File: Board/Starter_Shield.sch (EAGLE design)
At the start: 12 parts

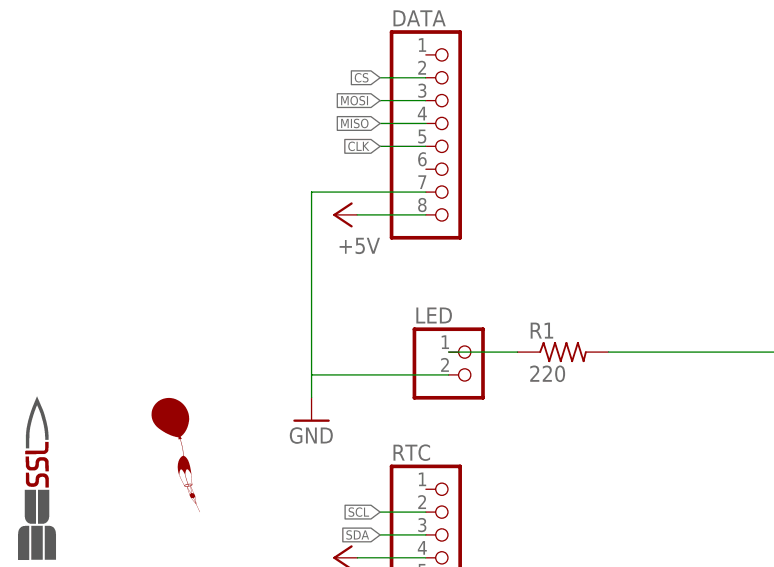
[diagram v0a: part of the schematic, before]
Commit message: updated gnd on the datalogger to the right pin - V1.2 now
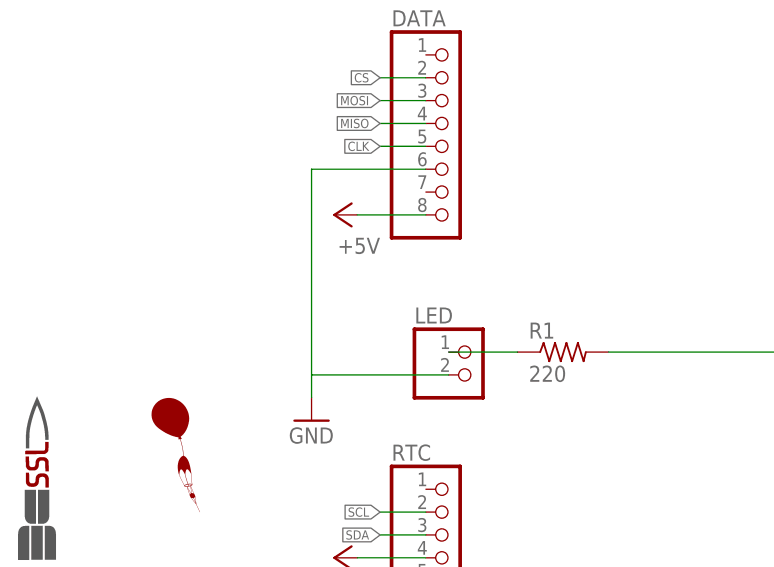
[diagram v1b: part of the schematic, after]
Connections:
- net GND: now also DATA.6; no longer DATA.7
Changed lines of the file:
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@@
 </segment>
 <segment>
-<pinref part="DATA" gate="A" pin="7"/>
-<wire x1="170.18" y1="93.98" x2="157.48" y2="93.98" width="0.1524" layer="91"/>
-<wire x1="157.48" y1="93.98" x2="157.48" y2="71.12" width="0.1524" layer="91"/>
+<wire x1="157.48" y1="96.52" x2="157.48" y2="71.12" width="0.1524" layer="91"/>
 <pinref part="GND3" gate="1" pin="GND"/>
+<pinref part="DATA" gate="A" pin="6"/>
+<wire x1="170.18" y1="96.52" x2="157.48" y2="96.52" width="0.1524" layer="91"/>
 </segment>
 </net>
